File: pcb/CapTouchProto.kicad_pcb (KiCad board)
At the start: 2 copper layers, 73.5 x 64 mm, 39 parts, among them J1 USB_C_Receptacle, J2 62684-50110, Q1 SS8050-G, Q2 SS8050-G, U1 CP2102N-A01-GQFN28, U2 1965-ESP32-WROOM-32E(8MB)CT-ND, U3 AMS1117-3.3

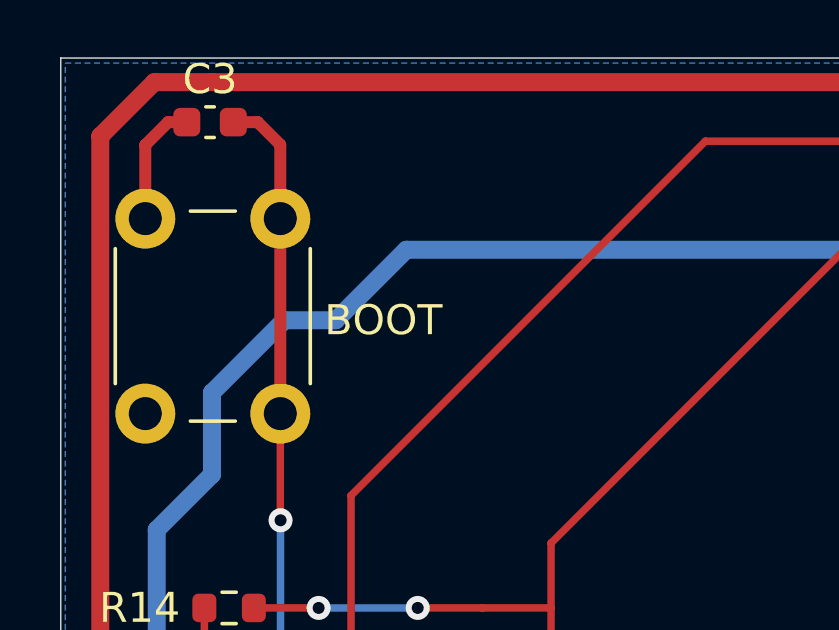
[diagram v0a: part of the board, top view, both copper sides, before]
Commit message: Specified 6mmx5mm tactile buttons.
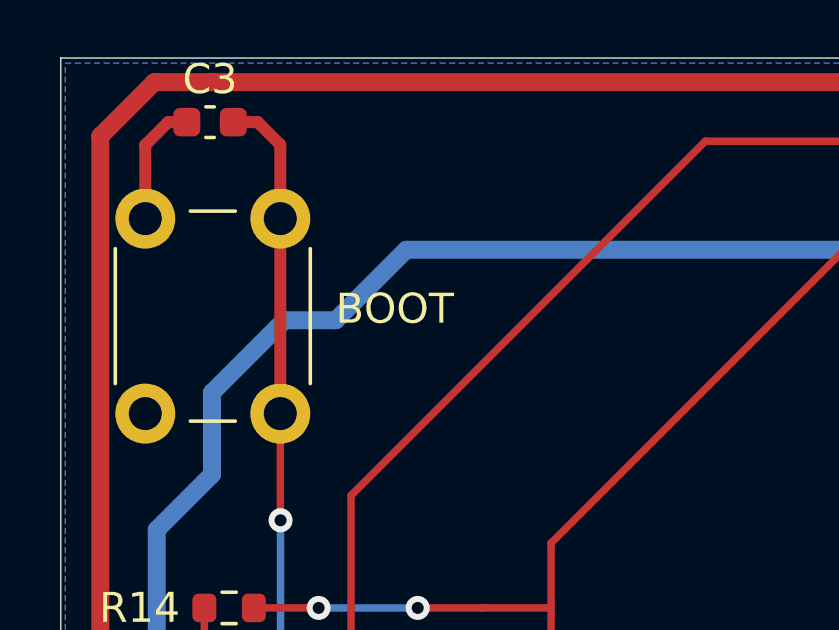
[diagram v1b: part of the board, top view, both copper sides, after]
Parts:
- removed the BOOT at (131.3, 89.9)
- removed the EN at (154.2, 132.8)
- added BOOT: SW_Push, Button_Switch_THT:SW_PUSH_6mm_H5mm, F.Cu at (131.3, 89.9)
- added EN: SW_Push, Button_Switch_THT:SW_PUSH_6mm_H5mm, F.Cu at (154.2, 132.8)

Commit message: Add test points.
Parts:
- added 3V3: 3V3, TestPoint:TestPoint_Pad_D2.5mm, F.Cu at (146.3, 138.4)
- added 5V: 5V, TestPoint:TestPoint_Pad_D2.5mm, F.Cu at (151.0, 138.4)
- added GND: Conn_01x01_Male, Connector_PinHeader_2.54mm:PinHeader_1x01_P2.54mm_Vertical, F.Cu at (155.1, 92.1)
- added SCL: SCL, TestPoint:TestPoint_Pad_D2.5mm, F.Cu at (197.8, 81.2)
- added SDA: SDA, TestPoint:TestPoint_Pad_D2.5mm, F.Cu at (192.6, 81.2)
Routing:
- net Net-(J2-Pad45): track 77.9 -> 80.8 mm
- net +3V3: track 230.5 -> 233.3 mm
- net VBUS: track 222.2 -> 224.6 mm
- net Net-(J2-Pad44): track 102.2 -> 102.8 mm
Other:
- board text added: "Author: cmumford"
- board text added: "Display Test"
- board text added: "JLCJLCJLCJLC"
- board text added: "rev. 1"
